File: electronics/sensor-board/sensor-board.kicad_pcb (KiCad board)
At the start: 4 copper layers, 176.6 x 134.6 mm, 193 parts, among them J10 Pressure_8, J11 Load_C_1, J12 Load_C_2, J13 Pressure_1, J14 Pressure_2, J15 Pressure_3, J16 Pressure_4, J17 Pressure_9, J18 Flow_1, J19 Flow_2, J24 CAN_Bus, J25 CAN_Bus, J26 Therm_1, J27 Therm_4, J28 Therm_7, J29 Therm_2, J3 SWD Header, J30 Therm_5, J31 Therm_3, J32 Therm_6, J4 Suppply_5V, J5 Supply_24V, J6 Supply_12V, J7 Pressure_5, J8 Pressure_6, J9 Pressure_7, SW1 SW_Push_Dual, U1 LD3985M33R_SOT23, U10 MCP96RL01T, U12 MAX44252ASD, U13 LMC6036, U14 LMC6036, U15 LMC6036, U16 MAX44252ASD, U2 STM32F105VBH6, U3 MAX33014EATB+, U4 MCP96RL01T, U5 MCP96RL01T, U6 MCP96RL01T, U7 MCP96RL01T, U8 MCP96RL01T, U9 MCP96RL01T, Y1 36 MHz

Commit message: Hole Location File Added
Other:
- board text added: "121 mm"
- board text added: "135 mm"
- board text added: "163 mm"
- board text added: "177.5 mm"
- board text added: "60.5 mm"
- board text added: "76.5 mm"
- board text removed: "121mm"
- board text removed: "163mm"
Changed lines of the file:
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@@
   (gr_line (start 72 160) (end 72 166) (layer "F.SilkS") (width 0.4))
   (gr_line (start 160.6356 63.742) (end 160.1856 64.292) (layer "F.SilkS") (width 0.15))
+  (gr_line (start 234.5 39) (end 234.5 18.5) (layer "Cmts.User") (width 0.15))
+  (gr_line (start 227 167) (end 254 167) (layer "Cmts.User") (width 0.15))
   (gr_line (start 227 178) (end 64 178) (layer "Cmts.User") (width 0.15))
   (gr_line (start 227 160) (end 227 180) (layer "Cmts.User") (width 0.15))
+  (gr_line (start 227 28) (end 150.5 28) (layer "Cmts.User") (width 0.15))
+  (gr_line (start 227 39) (end 227 24) (layer "Cmts.User") (width 0.15))
+  (gr_line (start 57 21.5) (end 234.5 21.5) (layer "Cmts.User") (width 0.15))
   (gr_line (start 64 39) (end 227 160) (layer "Cmts.User") (width 0.15))
   (gr_line (start 145.5 94) (end 150.5 94) (layer "Cmts.User") (width 0.15))
   (gr_line (start 64 160) (end 44 160) (layer "Cmts.User") (width 0.15))
+  (gr_line (start 150.5 99.5) (end 150.5 24) (layer "Cmts.User") (width 0.15))
   (gr_line (start 46 160) (end 46 39) (layer "Cmts.User") (width 0.15))
   (gr_line (start 145.5 99.5) (end 145.5 93.5) (layer "Cmts.User") (width 0.15))
   (gr_line (start 227 39) (end 64 160) (layer "Cmts.User") (width 0.15))
+  (gr_line (start 150.5 172.5) (end 227 172.5) (layer "Cmts.User") (width 0.15))
   (gr_line (start 150.5 99.5) (end 150.5 93.5) (layer "Cmts.User") (width 0.15))
+  (gr_line (start 227 160) (end 242 160) (layer "Cmts.User") (width 0.15))
+  (gr_line (start 238.5 99.5) (end 238.5 160) (layer "Cmts.User") (width 0.15))
   (gr_line (start 64 39) (end 44 39) (layer "Cmts.User") (width 0.15))
   (gr_line (start 64 160) (end 64 180) (layer "Cmts.User") (width 0.15))
+  (gr_line (start 57 39) (end 57 18.5) (layer "Cmts.User") (width 0.15))
+  (gr_line (start 248.5 32) (end 248.5 167) (layer "Cmts.User") (width 0.15))
+  (gr_line (start 227 32) (end 254 32) (layer "Cmts.User") (width 0.15))
+  (gr_line (start 150.5 99.5) (end 242 99.5) (layer "Cmts.User") (width 0.15))
+  (gr_line (start 150.5 99.5) (end 150.5 175) (layer "Cmts.User") (width 0.15))
   (gr_line (start 227 166.8) (end 64 166.8) (layer "Edge.Cuts") (width 0.1))
   (gr_arc (start 227 32.2) (mid 231.808326 34.191674) (end 233.8 39) (layer "Edge.Cuts") (width 0.1))
@@
     (effects (font (size 2 2) (thickness 0.5)) (justify left mirror))
   )
-  (gr_text "5mm right of center" (at 155 92.5) (layer "Cmts.User")
+  (gr_text "60.5 mm" (at 241 128 90) (layer "Cmts.User")
+    (effects (font (size 2 2) (thickness 0.3)))
+  )
+  (gr_text "76.5 mm" (at 181.5 174.5) (layer "Cmts.User")
+    (effects (font (size 2 2) (thickness 0.3)))
+  )
+  (gr_text "76.5 mm" (at 188.5 25.5) (layer "Cmts.User")
+    (effects (font (size 2 2) (thickness 0.3)))
+  )
+  (gr_text "135 mm\n" (at 251.5 98.5 90) (layer "Cmts.User")
+    (effects (font (size 2 2) (thickness 0.3)))
+  )
+  (gr_text "5mm right of center" (at 143 99.5) (layer "Cmts.User")
     (effects (font (size 1 1) (thickness 0.15)))
   )
-  (gr_text "121mm" (at 40.5 99.5 90) (layer "Cmts.User")
+  (gr_text "177.5 mm" (at 150.5 19) (layer "Cmts.User")
+    (effects (font (size 2 2) (thickness 0.3)))
+  )
+  (gr_text "121 mm" (at 40.5 99.5 90) (layer "Cmts.User")
     (effects (font (size 2 2) (thickness 0.4)))
   )
-  (gr_text "163mm" (at 145.5 182.5) (layer "Cmts.User")
+  (gr_text "163 mm" (at 145.5 182.5) (layer "Cmts.User")
     (effects (font (size 2 2) (thickness 0.4)))
   )

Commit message: work on BOM file
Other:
- board text added: "3.2 mm"
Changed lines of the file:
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@@
     )
   )
+  (gr_line (start 227 39) (end 240.5 39) (layer "B.Cu") (width 0.2))
   (gr_rect (start 73.4 51.3) (end 57.2 66.5) (layer "B.SilkS") (width 0.15) (fill none))
   (gr_rect (start 217.4 131.1) (end 233.8 141) (layer "B.SilkS") (width 0.15) (fill none))
@@
   (gr_arc (start 232.8 160) (mid 231.101219 164.101219) (end 227 165.8) (layer "Margin") (width 0.15))
   (gr_arc (start 227 33.2) (mid 231.101219 34.898781) (end 232.8 39) (layer "Margin") (width 0.15))
+  (gr_text "3.2 mm" (at 241 42) (layer "B.Cu")
+    (effects (font (size 2 2) (thickness 0.3)))
+  )
   (gr_text "Pressure\nTran. 7" (at 115 159) (layer "B.SilkS")
     (effects (font (size 2 2) (thickness 0.3)) (justify mirror))
@@
     (effects (font (size 2 2) (thickness 0.3)))
   )
-  (gr_text "5mm right of center" (at 143 99.5) (layer "Cmts.User")
-    (effects (font (size 1 1) (thickness 0.15)))
-  )
+  (gr_text "5mm right of center" (at 143 89.5) (layer "Cmts.User")
+    (effects (font (size 1 1) (thickness 0.15)))
+  )

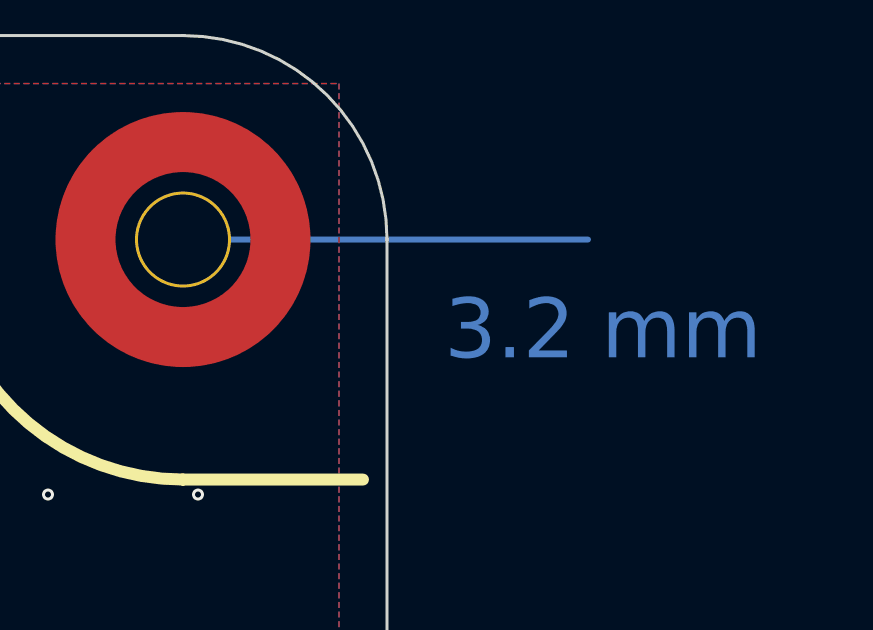
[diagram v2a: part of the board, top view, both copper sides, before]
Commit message: Added hole locations for output-board
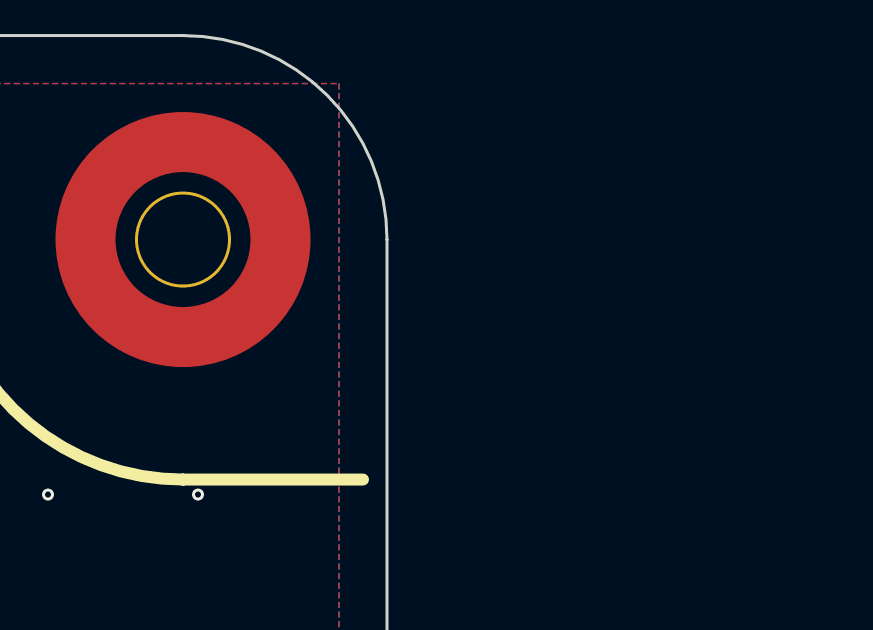
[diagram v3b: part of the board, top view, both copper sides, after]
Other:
- board text added: "3.2 mm (diamater, all holes)"
- board text removed: "3.2 mm"
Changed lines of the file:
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@@
     )
   )
-  (gr_line (start 227 39) (end 240.5 39) (layer "B.Cu") (width 0.2))
   (gr_rect (start 73.4 51.3) (end 57.2 66.5) (layer "B.SilkS") (width 0.15) (fill none))
   (gr_rect (start 217.4 131.1) (end 233.8 141) (layer "B.SilkS") (width 0.15) (fill none))
@@
   (gr_line (start 145.5 99.5) (end 145.5 93.5) (layer "Cmts.User") (width 0.15))
   (gr_line (start 227 39) (end 64 160) (layer "Cmts.User") (width 0.15))
+  (gr_line (start 227 39) (end 240.5 39) (layer "Cmts.User") (width 0.15))
   (gr_line (start 150.5 172.5) (end 227 172.5) (layer "Cmts.User") (width 0.15))
   (gr_line (start 150.5 99.5) (end 150.5 93.5) (layer "Cmts.User") (width 0.15))
@@
   (gr_arc (start 232.8 160) (mid 231.101219 164.101219) (end 227 165.8) (layer "Margin") (width 0.15))
   (gr_arc (start 227 33.2) (mid 231.101219 34.898781) (end 232.8 39) (layer "Margin") (width 0.15))
-  (gr_text "3.2 mm" (at 241 42) (layer "B.Cu")
-    (effects (font (size 2 2) (thickness 0.3)))
-  )
   (gr_text "Pressure\nTran. 7" (at 115 159) (layer "B.SilkS")
     (effects (font (size 2 2) (thickness 0.3)) (justify mirror))
@@
     (effects (font (size 2 2) (thickness 0.4)))
   )
+  (gr_text "3.2 mm (diamater, all holes)" (at 257 41.5) (layer "Cmts.User")
+    (effects (font (size 2 2) (thickness 0.3)))
+  )
   (segment (start 117.1356 86.542) (end 116.7356 86.142) (width 0.3) (layer "F.Cu") (net 1))

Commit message: update on BOM
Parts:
- R1: value 2.3k -> 3.2k
- R2: value 1k -> 100
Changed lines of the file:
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@@
       (effects (font (size 1 1) (thickness 0.15)))
     )
-    (fp_text value "2.3k" (at 0 1.43) (layer "F.Fab")
+    (fp_text value "3.2k" (at 0 1.43) (layer "F.Fab")
       (effects (font (size 1 1) (thickness 0.15)))
     )
@@
       (effects (font (size 1 1) (thickness 0.15)))
     )
-    (fp_text value "1k" (at 0 1.43) (layer "F.Fab")
+    (fp_text value "100" (at 0 1.43) (layer "F.Fab")
       (effects (font (size 1 1) (thickness 0.15)))
     )
@@
   (gr_line (start 72 160) (end 72 166) (layer "F.SilkS") (width 0.4))
   (gr_line (start 160.6356 63.742) (end 160.1856 64.292) (layer "F.SilkS") (width 0.15))
-  (gr_line (start 234.5 39) (end 234.5 18.5) (layer "Cmts.User") (width 0.15))
   (gr_line (start 227 167) (end 254 167) (layer "Cmts.User") (width 0.15))
+  (gr_line (start 234.5 39) (end 234.5 18.5) (layer "Cmts.User") (width 0.15))
   (gr_line (start 227 178) (end 64 178) (layer "Cmts.User") (width 0.15))
   (gr_line (start 227 160) (end 227 180) (layer "Cmts.User") (width 0.15))

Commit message: res value fix
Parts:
- R106: value 150 -> 100
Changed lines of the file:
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@@
       (effects (font (size 1 1) (thickness 0.15)))
     )
-    (fp_text value "150" (at 0 1.43 -90) (layer "F.Fab")
+    (fp_text value "100" (at 0 1.43 -90) (layer "F.Fab")
       (effects (font (size 1 1) (thickness 0.15)))
     )
